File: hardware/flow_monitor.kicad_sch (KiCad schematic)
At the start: 59 parts, among them J1 Conn_01x07_Pin, J5 Conn_01x02_Socket_TOP, J7 Conn_01x02_Socket_BOT, J8 Conn_01x06_Socket, Q1 2N7002, Q3 AO3401A, Q5 2N7002, Q6 2N7002, SW2 1TS005F-2500-5001, SW4 1TS005F-2500-5001, SW5 SK12D07VG5, U4 TPS610982DSET, U6 STM32G030C8Tx, U7 EA_DOGS164W-A, Y1 Crystal

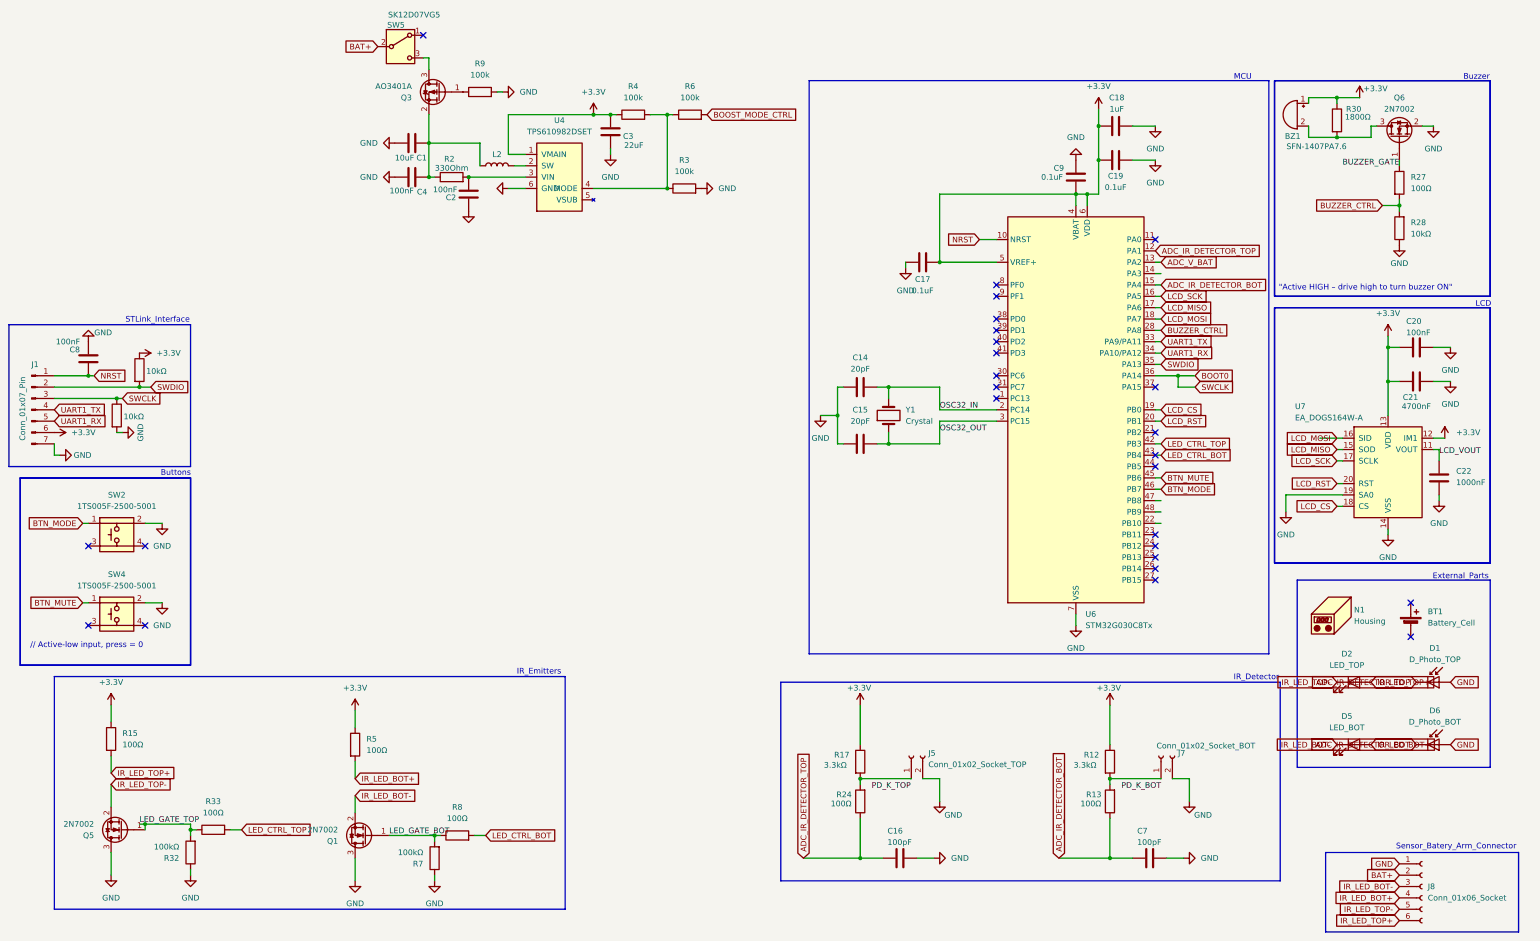
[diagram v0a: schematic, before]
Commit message: Add Rev-B hardware and firmware baseline
  - InfusionBA2: new STM32G071 project for Rev-B (dual photodiode, LPTIM1 Phase 2)
  - KiCad: Rev-B schematic + PCB (DOGS164, G071, TPS610981, COMP1 simplification)
  - Gerbers + STEP files from JLCPCB order W2026040304309275
  - Logo footprints (ETH, GHE) and generation script
  - Remove stale KiCad backup zips and lock files
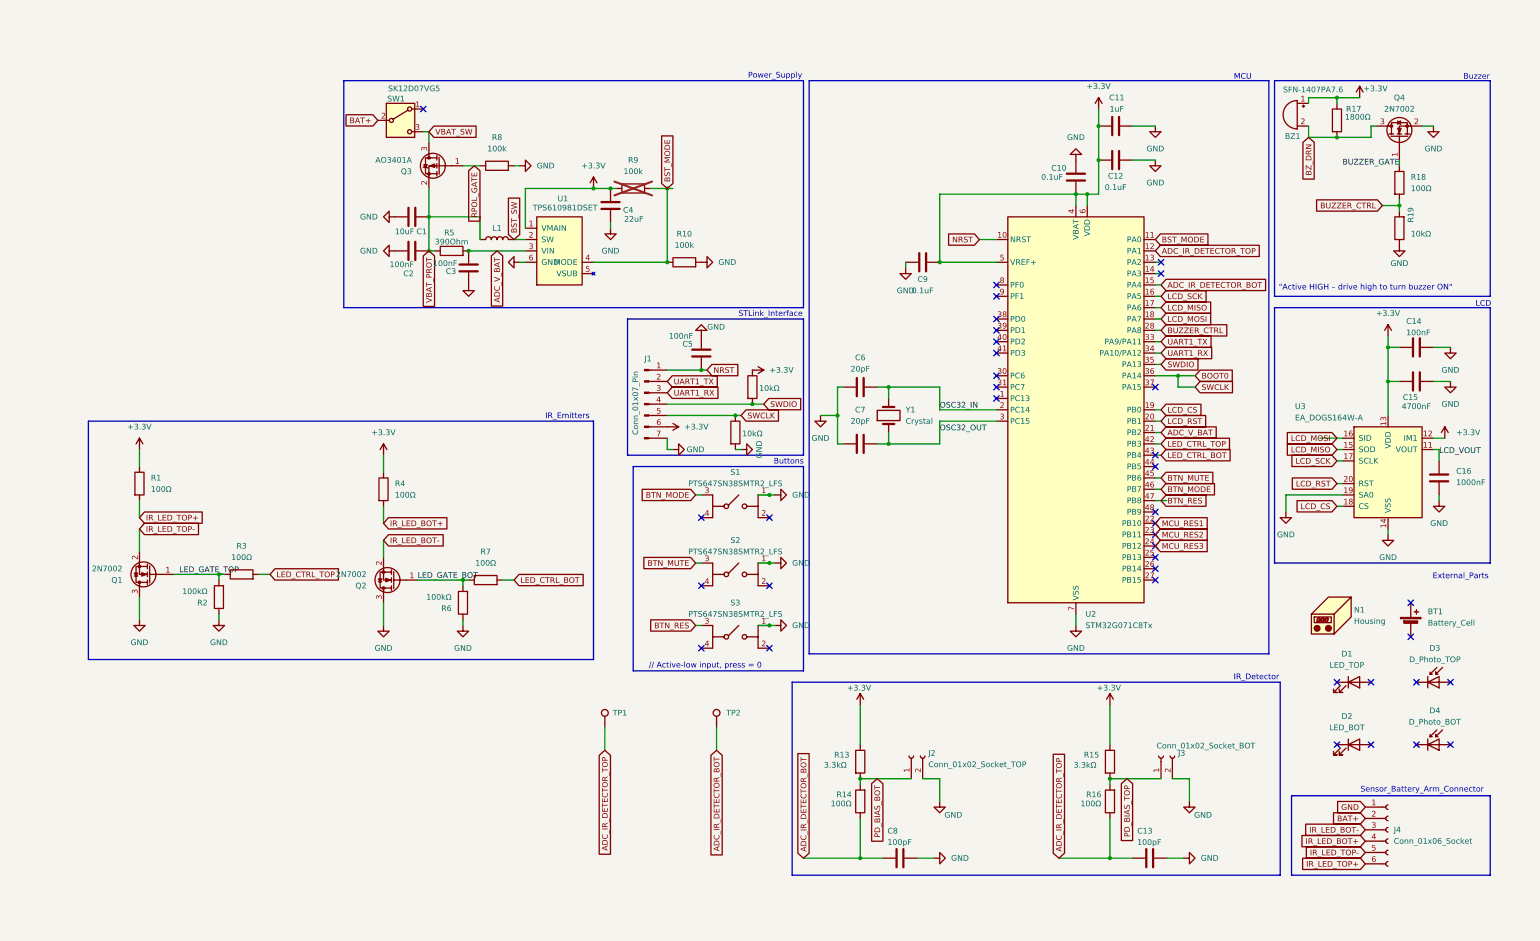
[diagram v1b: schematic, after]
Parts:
- removed R6: 100k, Resistor_SMD:R_0603_1608Metric, symbol Device:R
- removed SW2, SW4: 1TS005F-2500-5001, IV_Flow_Monitor_Footprints:SW_HYP_1TS005F-2500-5001, symbol IV_Flow_Monitor_Symbols:SW_HYP_1TS005F-2500-5001
- added S1, S2, S3: PTS647SN38SMTR2_LFS, Button_Switch_SMD:SW_SPST_PTS647_Sx38, symbol PTS647SN38SMTR2_LFS:PTS647SN38SMTR2_LFS
- added TP1, TP2: TestPoint, TestPoint:TestPoint_Keystone_5000-5004_Miniature, symbol Connector:TestPoint
- BZ1: LCSC (none) -> C360603; MPN (none) -> SFN-1407PA7.6
- C1: LCSC (none) -> C77041
- C10: renamed from C9; LCSC (none) -> C1591; MPN (none) -> CL10B104KB8NNNC
- C11: renamed from C18; LCSC (none) -> C15849; MPN (none) -> CL10A105KB8NNNC
- C12: renamed from C19; LCSC (none) -> C1591; MPN (none) -> CL10B104KB8NNNC
- C13: renamed from C7; LCSC (none) -> C14858; MPN (none) -> CL10C101JB8NNNC
- C14: renamed from C20; LCSC (none) -> C1591; MPN (none) -> CL10B104KB8NNNC
- C15: renamed from C21; LCSC (none) -> C19666; MPN (none) -> CL10A475KQ8NNNC
- C16: renamed from C22; LCSC (none) -> C15849; MPN (none) -> CL10A105KB8NNNC
- C2: renamed from C4; LCSC (none) -> C1590
- C3: renamed from C2; LCSC (none) -> C85864
- C4: renamed from C3; LCSC (none) -> C59461; MPN GRM21BR60J226ME39L -> CL10A226MQ8NRNC
- C5: renamed from C8; LCSC (none) -> C1591; MPN (none) -> CL10B104KB8NNNC
- C6: renamed from C14; LCSC (none) -> C1648; MPN (none) -> CL10C200JB8NNNC
- C7: renamed from C15; LCSC (none) -> C1648; MPN (none) -> CL10C200JB8NNNC
- C8: renamed from C16; LCSC (none) -> C14858; MPN (none) -> CL10C101JB8NNNC
- C9: renamed from C17; LCSC (none) -> C1591; MPN (none) -> CL10B104KB8NNNC
- J1: LCSC (none) -> C2897370
- J2: renamed from J5; footprint Connector_Wire:SolderWire-0.1sqmm_1x02_P3.6mm_D0.4mm_OD1mm_Relief -> Connector_PinSocket_2.54mm:PinSocket_1x02_P2.54mm_Vertical; LCSC (none) -> C49661
- J3: renamed from J7; footprint Connector_Wire:SolderWire-0.1sqmm_1x02_P3.6mm_D0.4mm_OD1mm_Relief -> Connector_PinSocket_2.54mm:PinSocket_1x02_P2.54mm_Vertical; LCSC (none) -> C49661
- L1: renamed from L2; footprint Inductor_SMD:L_0806_2016Metric -> Inductor_SMD:L_0805_2012Metric; LCSC (none) -> C86090; MPN DFE201612E-4R7M=P2 -> LQM21PN4R7MGRD
- Q1: renamed from Q5; LCSC (none) -> C8545; MPN (none) -> 2N7002
- Q2: renamed from Q1; LCSC (none) -> C8545; MPN (none) -> 2N7002
- Q3: LCSC (none) -> C347476
- Q4: renamed from Q6; LCSC (none) -> C8545; MPN (none) -> 2N7002
- R1: renamed from R15; LCSC (none) -> C22775; MPN (none) -> 0603WAF1000T5E
- R10: renamed from R3; LCSC (none) -> C25803; MPN RC0603FR-07100KL -> 0603WAF1003T5E
- R11: renamed from R1; LCSC (none) -> C25804; MPN (none) -> 0603WAF1002T5E
- R12: renamed from R16; LCSC (none) -> C25804; MPN (none) -> 0603WAF1002T5E
- R13: renamed from R17; LCSC (none) -> C22978; MPN (none) -> 0603WAF3301T5E
- R14: renamed from R24; LCSC (none) -> C22775; MPN (none) -> 0603WAF1000T5E
- R15: renamed from R12; LCSC (none) -> C22978; MPN (none) -> 0603WAF3301T5E
- R16: renamed from R13; LCSC (none) -> C22775; MPN (none) -> 0603WAF1000T5E
- R17: renamed from R30; LCSC (none) -> C4177; MPN (none) -> 0603WAF1801T5E
- R18: renamed from R27; LCSC (none) -> C22775; MPN (none) -> 0603WAF1000T5E
- R19: renamed from R28; LCSC (none) -> C25804; MPN (none) -> 0603WAF1002T5E
- R2: renamed from R32; LCSC (none) -> C25803; MPN (none) -> 0603WAF1003T5E
- R3: renamed from R33; LCSC (none) -> C22775; MPN (none) -> 0603WAF1000T5E
- R4: renamed from R5; LCSC (none) -> C22775; MPN (none) -> 0603WAF1000T5E
- R5: renamed from R2; value 330Ohm -> 390Ohm; LCSC (none) -> C137632; MPN RC0603JR-07330RL -> RC0603JR-07390RL
- R6: renamed from R7; LCSC (none) -> C25803; MPN (none) -> 0603WAF1003T5E
- R7: renamed from R8; LCSC (none) -> C22775; MPN (none) -> 0603WAF1000T5E
- R8: renamed from R9; LCSC (none) -> C25803; MPN RC0603FR-07100KL -> 0603WAF1003T5E
- R9: renamed from R4; MPN RC0603FR-07100KL -> 0603WAF1003T5E; now not fitted; now left out of the parts list
- SW1: renamed from SW5; footprint (none) -> IV_Flow_Monitor_Footprints:X_SW_Slide_SPDT_SSK12D07VG5; LCSC (none) -> C431548
- U1: renamed from U4; value TPS610982DSET -> TPS610981DSET; footprint Package_SON:Texas_DSE-6 -> TPS61098DSET:DSE0006A; symbol IV_Flow_Monitor_Symbols:TPS610982DSET -> IV_Flow_Monitor_Symbols:TPS610981DSET; LCSC (none) -> C73820; MPN TPS610982DSET -> TPS610981DSET
- U2: renamed from U6; value STM32G030C8Tx -> STM32G071C8Tx; symbol MCU_ST_STM32G0:STM32G030C8Tx -> MCU_ST_STM32G0:STM32G071C8Tx; LCSC (none) -> C529341; MPN (none) -> STM32G071C8T6
- U3: renamed from U7; footprint Display:EA_DOGS104X-A -> IV_Flow_Monitor_Footprints:EA_DOGS164X-A
- Y1: LCSC (none) -> C620155; MPN (none) -> X321532768KGD2SI
- renumbered D2 to D1, D5 to D2, D1 to D3, D6 to D4, J8 to J4
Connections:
- net ADC_IR_DETECTOR_BOT: now also C8.2, R14.1, TP2.1; no longer C13.2, D4.1 (K), R16.1
- net ADC_IR_DETECTOR_TOP: now also C13.2, R16.1, TP1.1; no longer C8.2, D3.1 (K), R14.1
- net ADC_V_BAT: now also C3.2, R5.2, U1.3 (VIN), U2.21 (PB2); no longer U2.13 (PA2)
- net BOOT0: now also J1.5 (Pin_5); no longer J1.3 (Pin_3)
- net BTN_MODE: now also S1.3 (COM_1)
- net BTN_MUTE: now also S2.3 (COM_1)
- net GND: now also S1.1 (NO_1), S2.1 (NO_1), S3.1 (NO_1); no longer D3.2 (A), D4.2 (A)
- net IR_LED_BOT+: no longer D2.2 (A)
- net IR_LED_BOT-: no longer D2.1 (K)
- net IR_LED_TOP+: no longer D1.2 (A)
- net IR_LED_TOP-: no longer D1.1 (K)
- net SWDIO: now also J1.4 (Pin_4); no longer J1.2 (Pin_2)
- net UART1_RX: now also J1.3 (Pin_3); no longer J1.5 (Pin_5)
- net UART1_TX: now also J1.2 (Pin_2); no longer J1.4 (Pin_4)
- net PD_BIAS_TOP: now reaches J3.1 (Pin_1), R15.2, R16.2
- net RPOL_GATE: now reaches Q3.1 (G), R8.1
- net VBAT_PROT: now reaches C1.1, C2.2, L1.1, Q3.2 (S), R5.1
- net VBAT_SW: now reaches Q3.3 (D), SW1.3 (C)
- net BZ_DRN: now reaches BZ1.2 (-), Q4.3 (D), R17.2
- net PD_BIAS_BOT: now reaches J2.1 (Pin_1), R13.2, R14.2
- net BST_SW: now reaches L1.2, U1.2 (SW)
- net BST_MODE: now reaches R10.1, R9.2, U1.4 (MODE)
- net BST_MODE: now also U2.11 (PA0)
- net MCU_RES1: now reaches U2.22 (PB10)
- net MCU_RES2: now reaches U2.23 (PB11)
- net MCU_RES3: now reaches U2.24 (PB12)
- net BTN_RES: now reaches U2.47 (PB8)
- net BTN_RES: now also S3.3 (COM_1)
- no-connect marks 26 -> 38
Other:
- note added: "Power_Supply"
- note added: "Sensor_Battery_Arm_Connector"
- note removed: "Sensor_Batery_Arm_Connector"
- moved on the sheet: C1, C2, C3, C4, C5, J1, J4, L1, Q1, Q2, Q3, R1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
